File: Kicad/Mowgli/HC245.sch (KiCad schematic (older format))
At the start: 4 parts, among them P1 Isolate

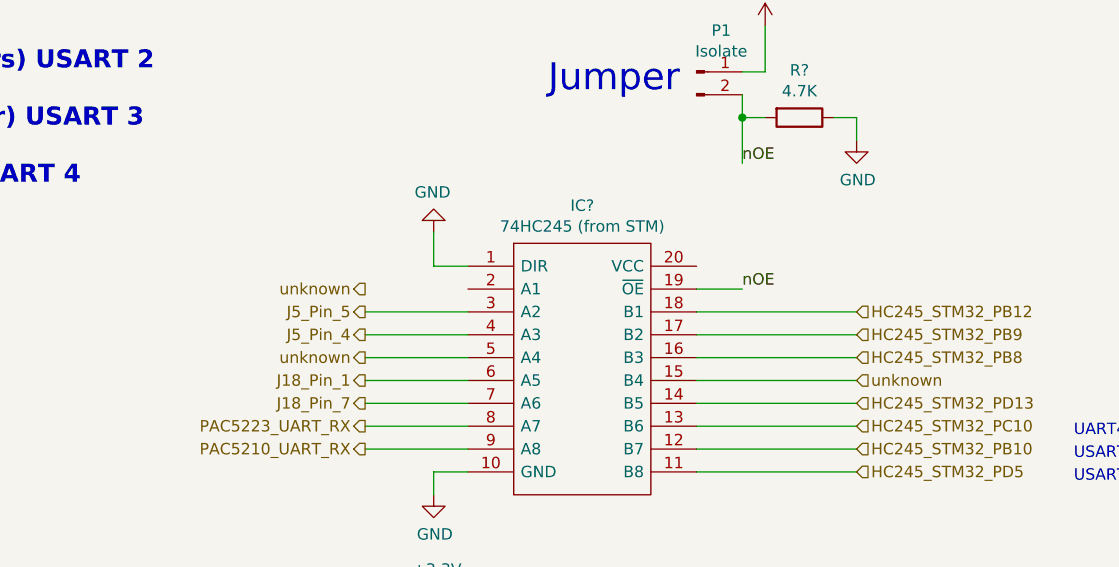
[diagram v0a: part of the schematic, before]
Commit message: reversed mechanical tilt and accelerometer circuit
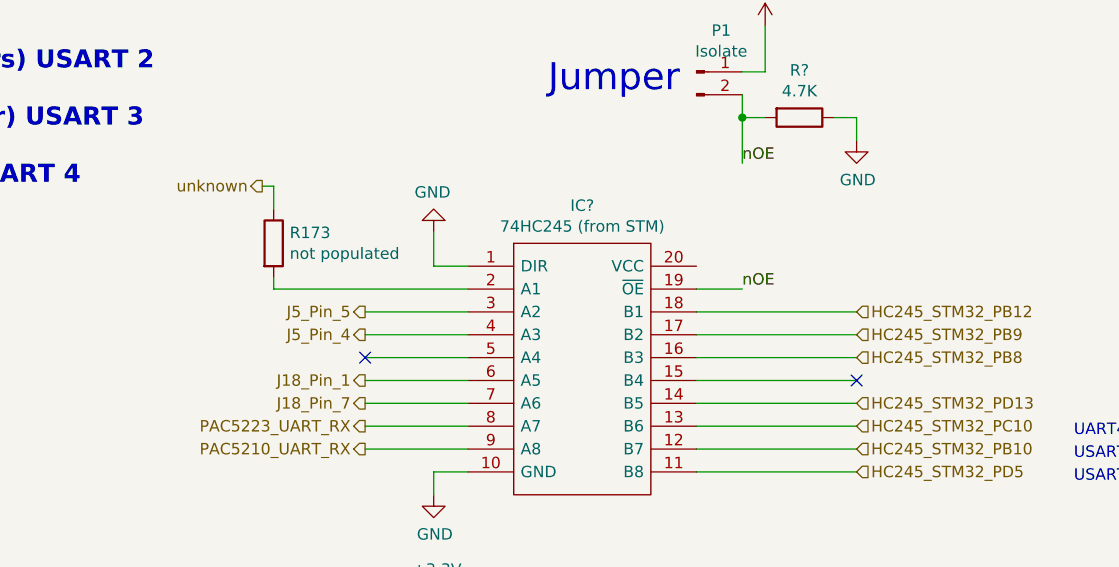
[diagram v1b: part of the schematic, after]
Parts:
- added R173: not populated, symbol Device:R
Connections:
- net unknown: now also R173.1; no longer IC?.15 (B4), IC?.5 (A4)
- net at IC?.2 (A1): now also R173.2
- no-connect marks 0 -> 2
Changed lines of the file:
@@
 $Descr A4 11693 8268
 encoding utf-8
-Sheet 9 14
+Sheet 8 14
 Title "Project Mowgli"
 Date "2022-05-22"
@@
 Wire Wire Line
 	6300 2300 5600 2300
-Text HLabel 4150 2200 0    50   Output ~ 0
+Text HLabel 3700 1750 0    50   Output ~ 0
 unknown
 Text HLabel 4150 2300 0    50   Output ~ 0
@@
 Text HLabel 4150 2400 0    50   Output ~ 0
 J5_Pin_4
-Text HLabel 4150 2500 0    50   Output ~ 0
-unknown
-Text HLabel 6300 2600 2    50   Input ~ 0
-unknown
 Wire Wire Line
 	6300 2600 5600 2600
@@
 Text Notes 4950 1350 0    118  ~ 0
 Jumper
+$Comp
+L Device:R R173
+U 1 1 62A909CA
+P 3750 2000
+F 0 "R173" H 3820 2046 50  0000 L CNN
+F 1 "not populated" H 3820 1955 50  0000 L CNN
+F 2 "" V 3680 2000 50  0001 C CNN
+F 3 "~" H 3750 2000 50  0001 C CNN
+	1    3750 2000
+	1    0    0    -1
+$EndComp
+Wire Wire Line
+	3750 2150 3750 2200
+Wire Wire Line
+	3750 2200 4600 2200
+NoConn ~ 6300 2600
+NoConn ~ 4150 2500
+Wire Wire Line
+	3700 1750 3750 1750
+Wire Wire Line
+	3750 1750 3750 1850
 $EndSCHEMATC
